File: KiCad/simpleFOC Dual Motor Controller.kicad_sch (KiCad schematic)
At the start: 1 part, among them U1 STM32F103C8Tx

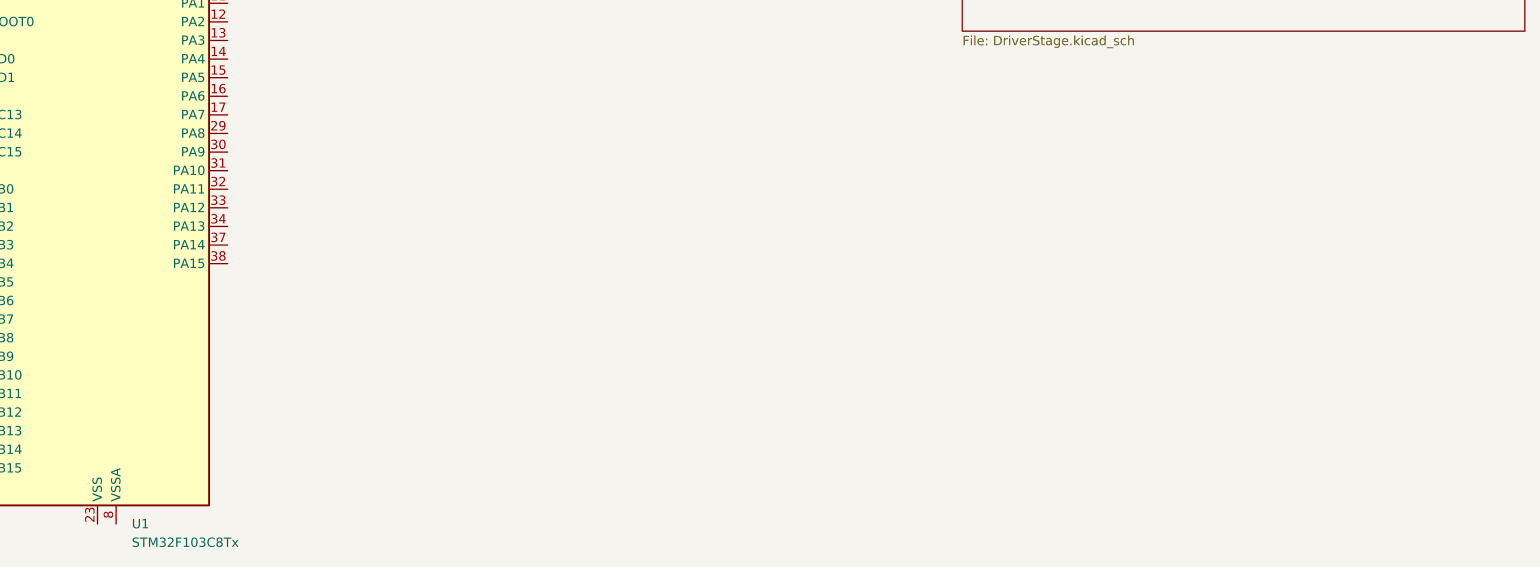
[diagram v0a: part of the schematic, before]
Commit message: High current drive routing
Add TDSON-8 3D models and footprint (.step, .wrl, .kicad_mod) and update easyeda2kicad library; modify KiCad schematic sheets (DriverStage.kicad_sch, PoleDriver.kicad_sch, simpleFOC Dual Motor Controller.kicad_sch) to reposition symbols/wires, add connector symbol instances, and refresh UUIDs and component references (e.g. C2/C3/U2 -> C202/C201/U201). Also update PCB and project files to reflect schematic changes so footprints and global labels stay in sync.
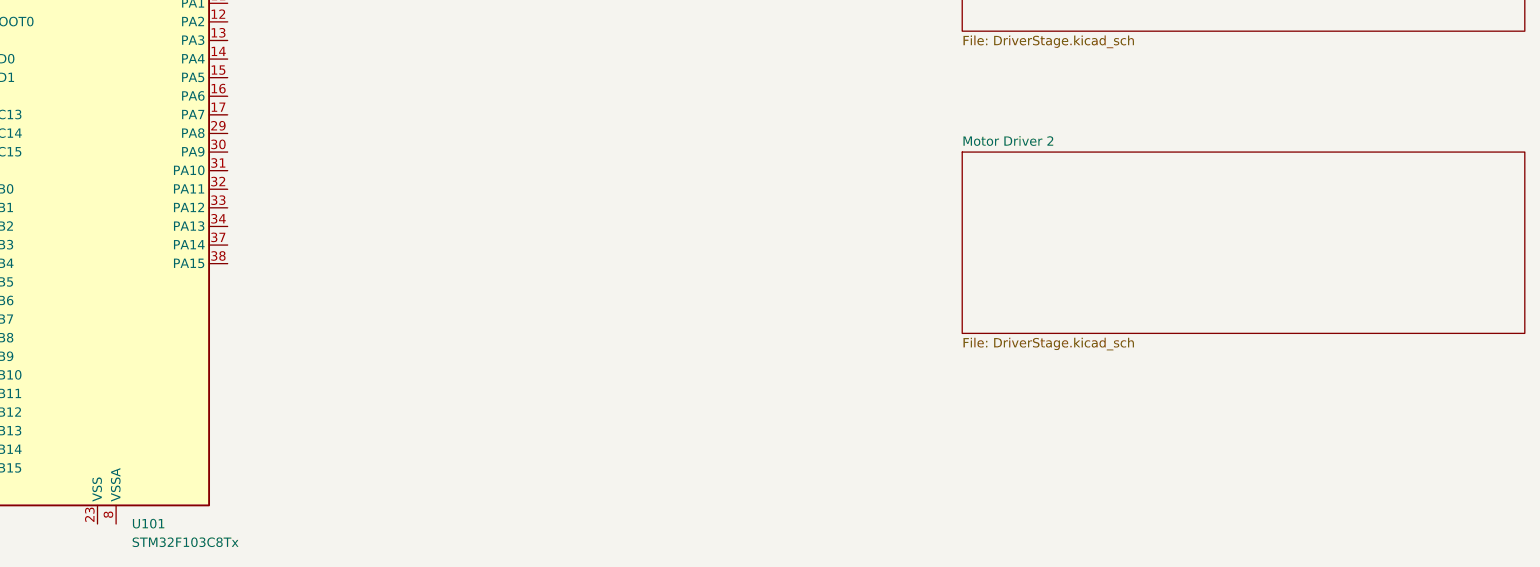
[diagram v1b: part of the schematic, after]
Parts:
- U101: renamed from U1; KiLib_Generator (none) -> package/gullwing
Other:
- added sheet Motor Driver 2 (DriverStage.kicad_sch)
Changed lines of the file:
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@@
 		(dnp no)
 		(fields_autoplaced yes)
-		(property "Reference" "U1"
+		(property "Reference" "U101"
 			(at 64.3733 133.35 0)
 			(show_name no)
@@
 		)
 		(property "Description" "STMicroelectronics Arm Cortex-M3 MCU, 64KB flash, 20KB RAM, 72 MHz, 2.0-3.6V, 37 GPIO, LQFP48"
+			(at 59.69 92.71 0)
+			(hide yes)
+			(show_name no)
+			(do_not_autoplace no)
+			(effects
+				(font
+					(size 1.27 1.27)
+				)
+			)
+		)
+		(property "KiLib_Generator" "package/gullwing"
 			(at 59.69 92.71 0)
 			(hide yes)
@@
 			(project "simpleFOC Dual Motor Controller"
 				(path "/0dffc378-5905-459a-b0cb-e8e514a8bbef"
-					(reference "U1")
+					(reference "U101")
 					(unit 1)
 				)
@@
 				)
 			)
+		)
+	)
+	(sheet
+		(at 177.8 82.55)
+		(size 76.835 24.765)
+		(exclude_from_sim no)
+		(in_bom yes)
+		(on_board yes)
+		(dnp no)
+		(fields_autoplaced yes)
+		(stroke
+			(width 0.1524)
+			(type solid)
+		)
+		(fill
+			(color 0 0 0 0)
+		)
+		(property "Sheetname" "Motor Driver 2"
+			(at 177.8 81.8384 0)
+			(show_name no)
+			(do_not_autoplace no)
+			(effects
+				(font
+					(size 1.27 1.27)
+				)
+				(justify left bottom)
+			)
+		)
+		(property "Sheetfile" "DriverStage.kicad_sch"
+			(at 177.8 107.8996 0)
+			(show_name no)
+			(do_not_autoplace no)
+			(effects
+				(font
+					(size 1.27 1.27)
+				)
+				(justify left top)
+			)
+		)
+		(instances
+			(project "simpleFOC Dual Motor Controller"
+				(path "/0dffc378-5905-459a-b0cb-e8e514a8bbef"
+					(page "6")
+				)
+			)

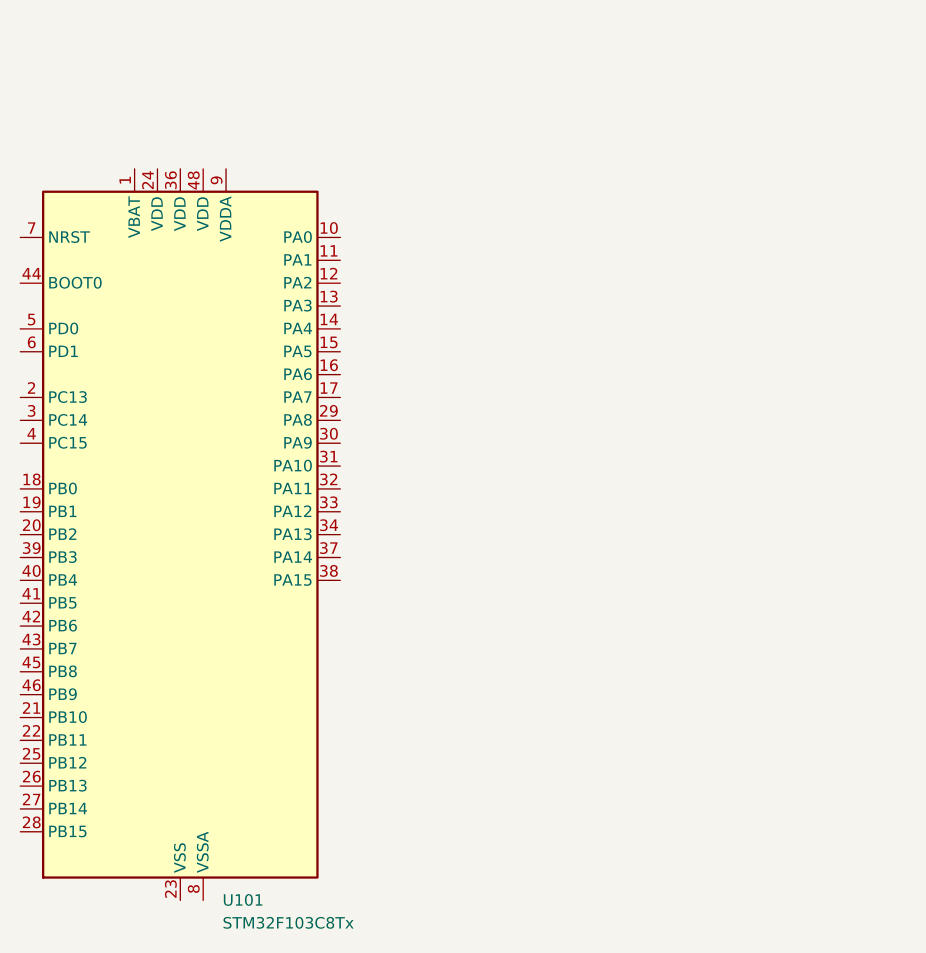
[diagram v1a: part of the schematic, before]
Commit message: Finished wiring motor drive circuitry
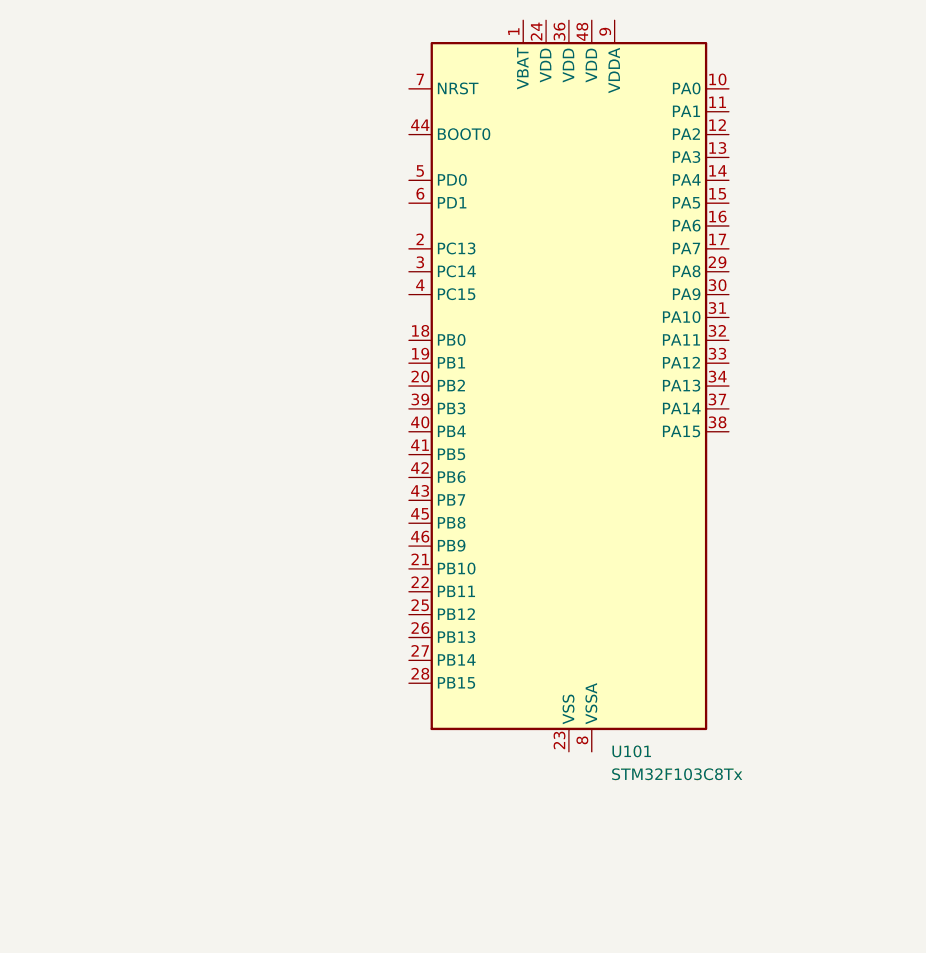
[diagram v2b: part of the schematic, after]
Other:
- moved on the sheet: U101
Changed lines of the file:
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@@
 	(symbol
 		(lib_id "MCU_ST_STM32F1:STM32F103C8Tx")
-		(at 59.69 92.71 0)
+		(at 102.87 76.2 0)
 		(unit 1)
 		(body_style 1)
@@
 		(fields_autoplaced yes)
 		(property "Reference" "U101"
-			(at 64.3733 133.35 0)
+			(at 107.5533 116.84 0)
 			(show_name no)
 			(do_not_autoplace no)
@@
 		)
 		(property "Value" "STM32F103C8Tx"
-			(at 64.3733 135.89 0)
+			(at 107.5533 119.38 0)
 			(show_name no)
 			(do_not_autoplace no)
@@
 		)
 		(property "Footprint" "Package_QFP:LQFP-48_7x7mm_P0.5mm"
-			(at 44.45 130.81 0)
+			(at 87.63 114.3 0)
 			(hide yes)
 			(show_name no)
@@
 		)
 		(property "Datasheet" "https://www.st.com/resource/en/datasheet/stm32f103c8.pdf"
-			(at 59.69 92.71 0)
+			(at 102.87 76.2 0)
 			(hide yes)
 			(show_name no)
@@
 		)
 		(property "Description" "STMicroelectronics Arm Cortex-M3 MCU, 64KB flash, 20KB RAM, 72 MHz, 2.0-3.6V, 37 GPIO, LQFP48"
-			(at 59.69 92.71 0)
+			(at 102.87 76.2 0)
 			(hide yes)
 			(show_name no)
@@
 		)
 		(property "KiLib_Generator" "package/gullwing"
-			(at 59.69 92.71 0)
+			(at 102.87 76.2 0)
 			(hide yes)
 			(show_name no)

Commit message: started adding supporting components
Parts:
- added C101: 470u, symbol Device:C_Polarized_Small
- added C102: 4.7u, symbol Device:C_Small
- added C103, C104, C105, C106, C107: 100n, symbol Device:C_Small
- added CN101: MR60-F, easyeda2kicad:CONN-TH_3P-P5.50_MR60-F, symbol easyeda2kicad:MR60-F
- added D101: SMAJ36A, Diode_SMD:D_SMA, symbol Diode:SMAJ36A
- added D103: DSK26_C7502712, easyeda2kicad:SOD-123FL_L2.7-W1.8-LS3.8-RD, symbol easyeda2kicad:DSK26_C7502712
- added D104: SMF5.0A_C19077497, easyeda2kicad:SOD-123FL_L2.7-W1.8-LS3.8-RD, symbol easyeda2kicad:SMF5.0A_C19077497
- added H101, H102: MountingHole, MountingHole:MountingHole_4.3mm_M4, symbol Mechanical:MountingHole
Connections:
- net +3.3V: now reaches U101.1 (VBAT)
- net +3.3V: now also U101.24 (VDD), U101.36 (VDD), U101.48 (VDD), U101.9 (VDDA), C102.1, C103.1, C104.1, C105.1, C106.1, C107.1, D103.1 (K)
- net GND: now reaches U101.23 (VSS), U101.35 (VSS), U101.47 (VSS)
- net GND: now also U101.8 (VSSA), C101.2, C102.2, C103.2, C104.2, C105.2, C106.2, C107.2, CN101.2, D101.2 (A2), D104.2 (A)
- new net: CN101.1, D103.2 (A), D104.1 (K)
- new net Motor Driver 1/Motor_VIN: C101.1, CN101.3, D101.1 (A1)
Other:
- sheet Motor Driver 1 ports: added Motor_VIN; removed none
- sheet Motor Driver 2 ports: added Motor_VIN; removed none
- moved on the sheet: U101

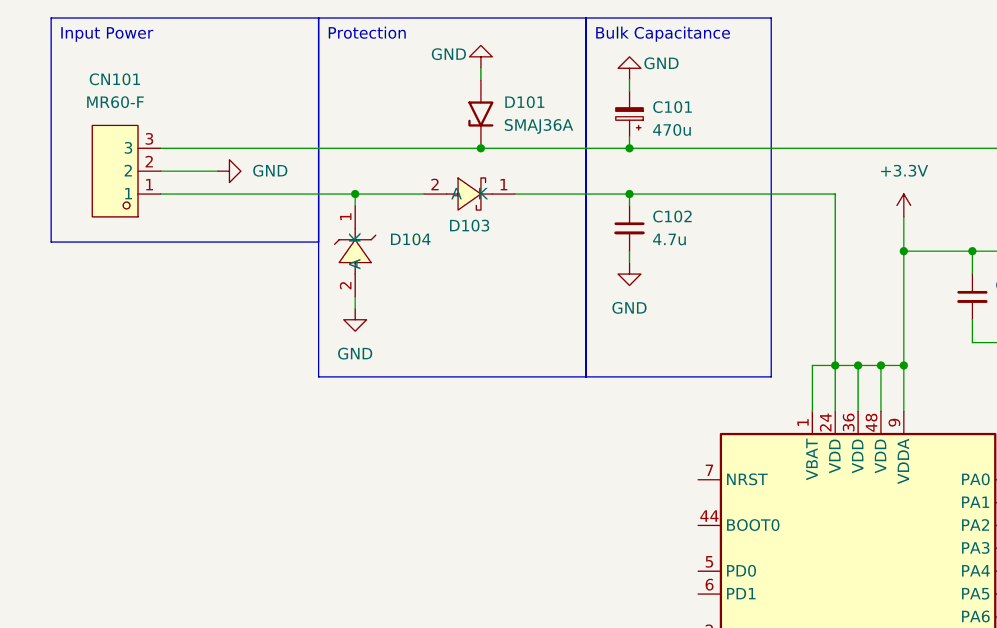
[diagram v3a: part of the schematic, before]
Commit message: rewired the board with smaller mosfets
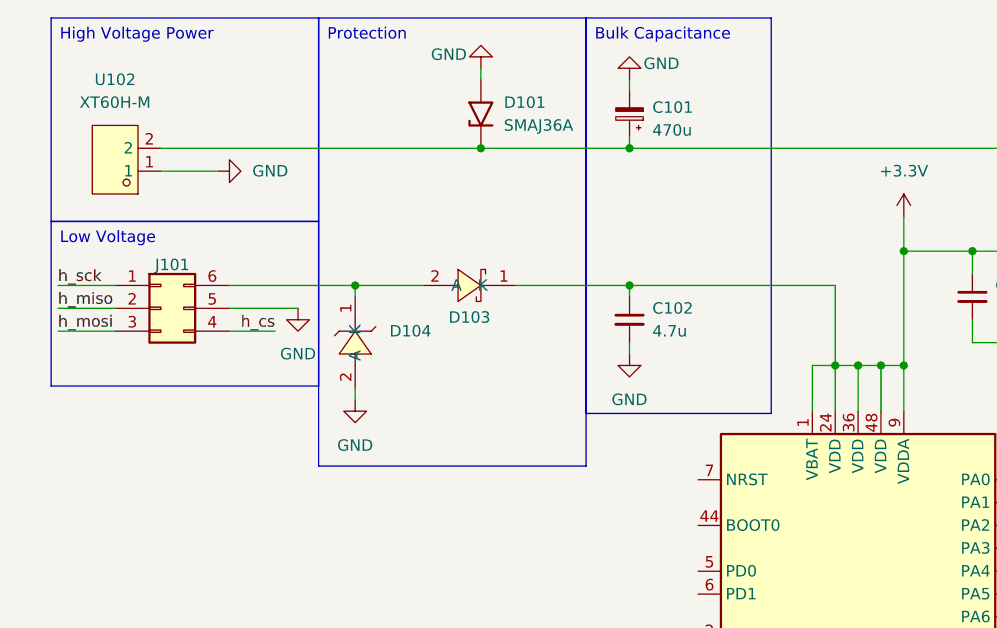
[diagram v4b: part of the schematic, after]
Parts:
- removed CN101: MR60-F, easyeda2kicad:CONN-TH_3P-P5.50_MR60-F, symbol easyeda2kicad:MR60-F
- added J101: Conn_02x03_Counter_Clockwise, symbol Connector_Generic:Conn_02x03_Counter_Clockwise
- added U102: XT60H-M, easyeda2kicad:CONN-TH_XT60H-M, symbol easyeda2kicad:XT60H-M
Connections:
- net GND: now also J101.5 (Pin_5), U102.1
- net Motor Driver 1/Motor_VIN: now also U102.2
- net at D103.2 (A), D104.1 (K): now also J101.6 (Pin_6)
- new net h_cs: J101.4 (Pin_4)
- new net h_miso: J101.2 (Pin_2)
- new net h_mosi: J101.3 (Pin_3)
- new net h_sck: J101.1 (Pin_1)
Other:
- moved on the sheet: C102, D103, D104

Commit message: start adding control pins
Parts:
- removed J101: Conn_02x03_Counter_Clockwise, symbol Connector_Generic:Conn_02x03_Counter_Clockwise
- added J101: Conn_01x04, PCM_SparkFun-Connector:JST_1x04_P2.0mm_Vertical_PTH, symbol PCM_SparkFun-Connector:Conn_01x04_JST_P2.0mm_Vertical_PTH
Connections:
- net GND: now also J101.3 (Pin_3)
- net at D103.2 (A), D104.1 (K): now also J101.4 (Pin_4)
- net snsA2: now reaches U101.10 (PA0)
- net snsB2: now reaches U101.11 (PA1)
- net snsC2: now reaches U101.12 (PA2)
- net snsA1: now reaches U101.14 (PA4)
- net snsB1: now reaches U101.18 (PB0)
- net snsC1: now reaches U101.19 (PB1)
- net CHAn1: now reaches U101.26 (PB13)
- net CHBn1: now reaches U101.27 (PB14)
- net CHCn1: now reaches U101.28 (PB15)
- net CHA1: now reaches U101.29 (PA8)
- net CHB1: now reaches U101.30 (PA9)
- net CHC1: now reaches U101.31 (PA10)
- net CHA2: now reaches U101.38 (PA15)
- net CHAn2: now reaches U101.39 (PB3)
- net CHB2: now reaches U101.40 (PB4)
- net CHBn2: now reaches U101.41 (PB5)
- net CHC2: now reaches U101.42 (PB6)
- net CHCn2: now reaches U101.43 (PB7)
- net h_scl: now reaches U101.45 (PB8)
- net h_scl: now also J101.1 (Pin_1)
- net h_sda: now reaches U101.46 (PB9)
- net h_sda: now also J101.2 (Pin_2)
- net Motor Driver 1/Motor_VIN renamed M+
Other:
- sheet Motor Driver 1 ports: added CAL, EN, FAULT, INHA, INHB, INHC, INLA, INLB, INLC, SOA, SOB, SOC; removed none
- sheet Motor Driver 2 ports: added CAL, EN, FAULT, INHA, INHB, INHC, INLA, INLB, INLC, SOA, SOB, SOC; removed none
- moved on the sheet: C101, C102, C103, C104, C105, C106, C107, D101, D103, D104, U101, U102
